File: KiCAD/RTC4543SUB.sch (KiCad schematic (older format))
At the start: 22 parts, among them J1 YM2203-B A-CON, J2 RTC-4543SA Mod, J3 I2C(Grove), J4 YM2203-B B-CON, Q1 2N7000, Q2 2N7000, U1 74HC07, U2 LP2950-3.3_TO92

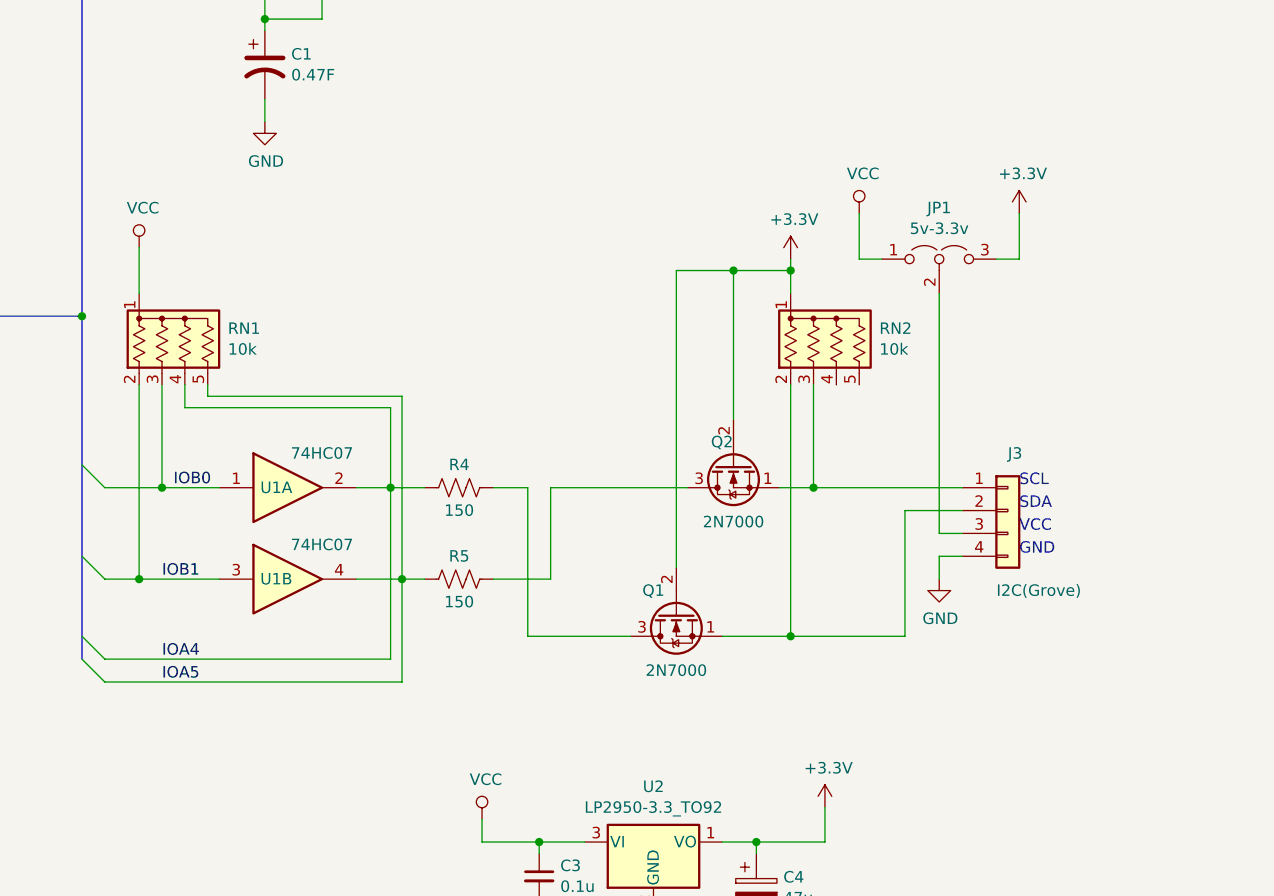
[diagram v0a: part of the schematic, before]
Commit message: I2C 電圧レベル変換を秋月電子AE-PCA9306モジュールへ変更
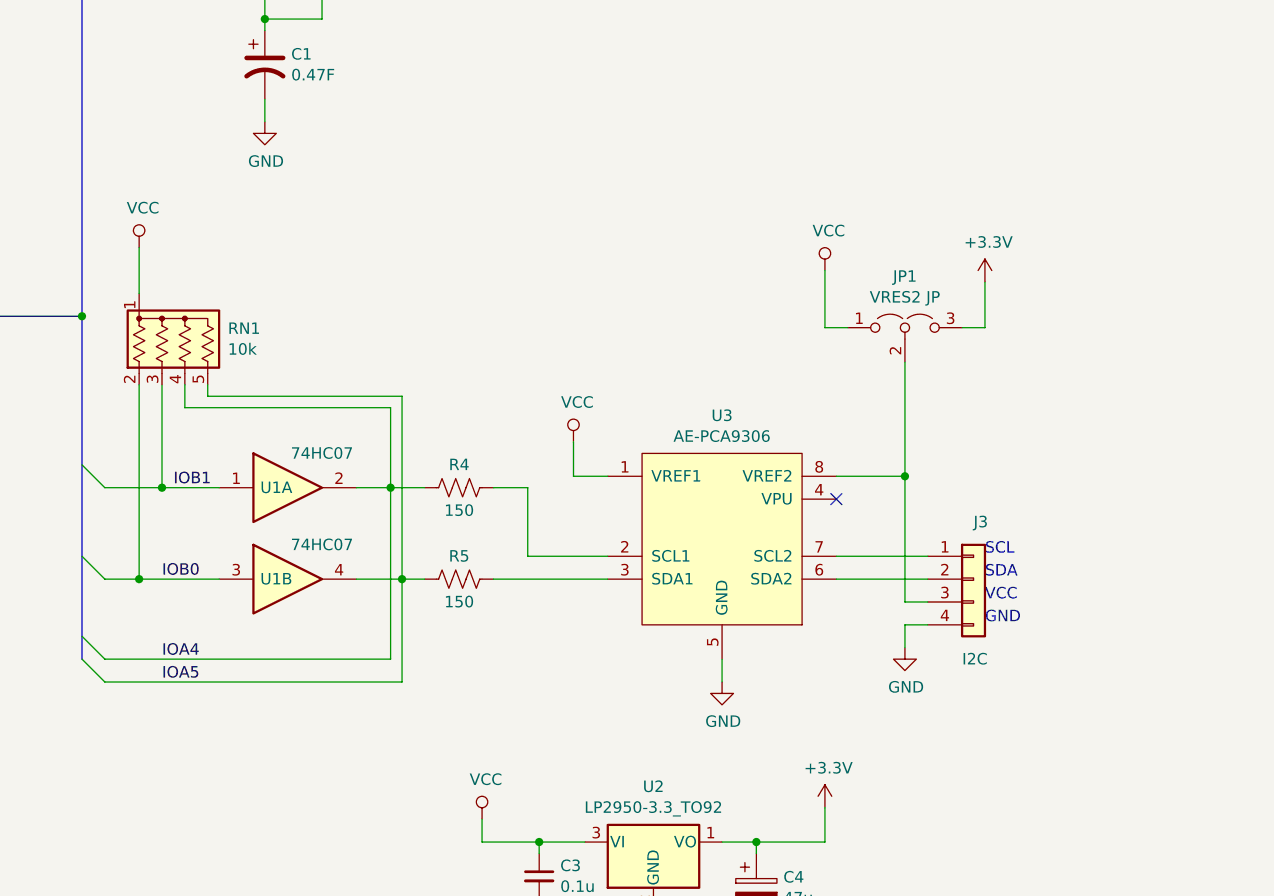
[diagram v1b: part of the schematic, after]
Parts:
- removed Q1, Q2: 2N7000, Package_TO_SOT_THT:TO-92_Inline, symbol Transistor_FET:2N7000
- removed RN2: 10k, Resistor_THT:R_Array_SIP5, symbol Device:R_Network04_US
- added U3: AE-PCA9306, symbol AE-PCA9306:AE-PCA9306
- J3: value I2C(Grove) -> I2C
- JP1: value 5v-3.3v -> VRES2 JP
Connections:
- net GND: now also U3.5 (GND)
- net IOB0: now also RN1.2 (R1), U1.3; no longer RN1.3 (R2), U1.1
- net IOB1: now also RN1.3 (R2), U1.1; no longer RN1.2 (R1), U1.3
- net VCC: now also U3.1 (VREF1)
- net at J3.1 (Pin_1): now also U3.7 (SCL2)
- net at J3.2 (Pin_2): now also U3.6 (SDA2)
- net at J3.3 (Pin_3), JP1.2 (C): now also U3.8 (VREF2)
- net at R4.1: now also U3.2 (SCL1)
- net at R5.1: now also U3.3 (SDA1)
- no-connect marks 24 -> 25
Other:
- moved on the sheet: J3
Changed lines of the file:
@@
 $EndComp
 Wire Wire Line
-	6350 5700 6350 5800
-Wire Wire Line
-	6450 5700 6350 5700
-Wire Wire Line
-	6350 5600 6450 5600
-$Comp
-L power:VCC #PWR09
-U 1 1 607028FD
-P 6000 4200
-F 0 "#PWR09" H 6000 4050 50  0001 C CNN
-F 1 "VCC" H 6017 4373 50  0000 C CNN
-F 2 "" H 6000 4200 50  0001 C CNN
-F 3 "" H 6000 4200 50  0001 C CNN
-	1    6000 4200
-	1    0    0    -1
-$EndComp
-Wire Wire Line
-	4650 5800 4650 5400
-Wire Wire Line
-	4400 5800 4650 5800
-Wire Wire Line
-	6200 5500 6450 5500
+	6200 6000 6200 6100
+Wire Wire Line
+	6300 6000 6200 6000
+Wire Wire Line
+	6200 5900 6300 5900
 Wire Wire Line
 	4400 5400 4550 5400
@@
 IOA5
 Text Label 2950 5800 0    50   ~ 0
-IOB1
+IOB0
 Wire Wire Line
 	2700 5800 2850 5800
@@
 IOA4
 Text Label 3000 5400 0    50   ~ 0
-IOB0
+IOB1
 Wire Wire Line
 	2700 5400 2950 5400
@@
 L power:GND #PWR010
 U 1 1 606C2B45
-P 6350 5800
-F 0 "#PWR010" H 6350 5550 50  0001 C CNN
-F 1 "GND" H 6355 5627 50  0000 C CNN
-F 2 "" H 6350 5800 50  0001 C CNN
-F 3 "" H 6350 5800 50  0001 C CNN
-	1    6350 5800
+P 6200 6100
+F 0 "#PWR010" H 6200 5850 50  0001 C CNN
+F 1 "GND" H 6205 5927 50  0000 C CNN
+F 2 "" H 6200 6100 50  0001 C CNN
+F 3 "" H 6200 6100 50  0001 C CNN
+	1    6200 6100
 	1    0    0    -1
 $EndComp
@@
 	1    0    0    -1
 $EndComp
-Text Notes 6700 5700 0    50   ~ 0
+Text Notes 6550 6000 0    50   ~ 0
 GND
-Text Notes 6700 5600 0    50   ~ 0
+Text Notes 6550 5900 0    50   ~ 0
 VCC
-Text Notes 6700 5500 0    50   ~ 0
+Text Notes 6550 5800 0    50   ~ 0
 SDA
-Text Notes 6700 5400 0    50   ~ 0
+Text Notes 6550 5700 0    50   ~ 0
 SCL
 $Comp
 L Connector_Generic:Conn_01x04 J3
 U 1 1 606BD3C7
-P 6650 5500
-F 0 "J3" H 6650 5750 50  0000 L CNN
-F 1 "I2C(Grove)" H 6600 5150 50  0000 L CNN
-F 2 "Connectors:Grove_1x04" H 6650 5500 50  0001 C CNN
-F 3 "~" H 6650 5500 50  0001 C CNN
-	1    6650 5500
+P 6500 5800
+F 0 "J3" H 6500 6050 50  0000 L CNN
+F 1 "I2C" H 6450 5450 50  0000 L CNN
+F 2 "Connectors:Grove_1x04" H 6500 5800 50  0001 C CNN
+F 3 "~" H 6500 5800 50  0001 C CNN
+	1    6500 5800
 	1    0    0    -1
 $EndComp
@@
 	1    0    0    -1
 $EndComp
-$Comp
-L Transistor_FET:2N7000 Q1
-U 1 1 6076870C
-P 5200 5950
-F 0 "Q1" V 5100 6050 50  0000 C CNN
-F 1 "2N7000" V 5450 5950 50  0000 C CNN
-F 2 "Package_TO_SOT_THT:TO-92_Inline" H 5400 5875 50  0001 L CIN
-F 3 "https://www.fairchildsemi.com/datasheets/2N/2N7000.pdf" H 5200 5950 50  0001 L CNN
-	1    5200 5950
-	0    -1   1    0
-$EndComp
-$Comp
-L power:+3.3V #PWR0103
-U 1 1 6076E120
-P 5700 4400
-F 0 "#PWR0103" H 5700 4250 50  0001 C CNN
-F 1 "+3.3V" H 5715 4573 50  0000 C CNN
-F 2 "" H 5700 4400 50  0001 C CNN
-F 3 "" H 5700 4400 50  0001 C CNN
-	1    5700 4400
-	1    0    0    -1
-$EndComp
-$Comp
-L Device:R_Network04_US RN2
-U 1 1 6076FE3F
-P 5900 4750
-F 0 "RN2" H 6088 4796 50  0000 L CNN
-F 1 "10k" H 6088 4705 50  0000 L CNN
-F 2 "Resistor_THT:R_Array_SIP5" V 6175 4750 50  0001 C CNN
-F 3 "http://www.vishay.com/docs/31509/csc.pdf" H 5900 4750 50  0001 C CNN
-	1    5900 4750
-	1    0    0    -1
-$EndComp
-$Comp
-L Transistor_FET:2N7000 Q2
-U 1 1 60777F0B
-P 5450 5300
-F 0 "Q2" V 5350 5350 50  0000 C CNN
-F 1 "2N7000" V 5700 5300 50  0000 C CNN
-F 2 "Package_TO_SOT_THT:TO-92_Inline" H 5650 5225 50  0001 L CIN
-F 3 "https://www.fairchildsemi.com/datasheets/2N/2N7000.pdf" H 5450 5300 50  0001 L CNN
-	1    5450 5300
-	0    -1   1    0
-$EndComp
-Wire Wire Line
-	4550 6050 5000 6050
-Wire Wire Line
-	4550 5400 4550 6050
-Wire Wire Line
-	4650 5400 5250 5400
+Wire Wire Line
+	4550 5400 4550 5700
 $Comp
 L power:+3.3V #PWR0104
 U 1 1 607AE270
-P 6700 4200
-F 0 "#PWR0104" H 6700 4050 50  0001 C CNN
-F 1 "+3.3V" H 6715 4373 50  0000 C CNN
-F 2 "" H 6700 4200 50  0001 C CNN
-F 3 "" H 6700 4200 50  0001 C CNN
-	1    6700 4200
-	1    0    0    -1
-$EndComp
-$Comp
-L Jumper:Jumper_3_Open JP1
-U 1 1 607AF803
-P 6350 4400
-F 0 "JP1" H 6350 4624 50  0000 C CNN
-F 1 "5v-3.3v" H 6350 4533 50  0000 C CNN
-F 2 "" H 6350 4400 50  0001 C CNN
-F 3 "~" H 6350 4400 50  0001 C CNN
-	1    6350 4400
-	1    0    0    -1
-$EndComp
-Wire Wire Line
-	6000 4200 6000 4400
-Wire Wire Line
-	6700 4400 6700 4200
+P 6550 4500
+F 0 "#PWR0104" H 6550 4350 50  0001 C CNN
+F 1 "+3.3V" H 6565 4673 50  0000 C CNN
+F 2 "" H 6550 4500 50  0001 C CNN
+F 3 "" H 6550 4500 50  0001 C CNN
+	1    6550 4500
+	1    0    0    -1
+$EndComp
+Wire Wire Line
+	6550 4700 6550 4500
 $Comp
 L power:+3.3V #PWR0105
@@
 $EndComp
 Wire Wire Line
-	6200 5500 6200 6050
-Wire Wire Line
-	5650 5400 5800 5400
-Wire Wire Line
-	5700 4400 5700 4450
-Wire Wire Line
-	5800 4950 5800 5400
-Connection ~ 5800 5400
-Wire Wire Line
-	5800 5400 6450 5400
-Connection ~ 5700 6050
-Wire Wire Line
-	5700 6050 6200 6050
-Wire Wire Line
-	5400 6050 5700 6050
-Wire Wire Line
-	5450 5100 5450 4450
-Wire Wire Line
-	5450 4450 5700 4450
-Connection ~ 5700 4450
-Wire Wire Line
-	5700 4450 5700 4550
-Wire Wire Line
-	5450 4450 5200 4450
-Wire Wire Line
-	5200 4450 5200 5750
-Connection ~ 5450 4450
-Wire Wire Line
-	5700 4950 5700 6050
-Wire Wire Line
-	6000 4400 6100 4400
-Wire Wire Line
-	6600 4400 6700 4400
-Wire Wire Line
-	6350 4550 6350 5600
+	6450 4700 6550 4700
 $Comp
 L Regulator_Linear:LP2950-3.3_TO92 U2
@@
 NoConn ~ 1700 5150
 Connection ~ 2600 4650
+$Comp
+L power:VCC #PWR09
+U 1 1 607ACB7D
+P 4750 5200
+F 0 "#PWR09" H 4750 5050 50  0001 C CNN
+F 1 "VCC" H 4767 5373 50  0000 C CNN
+F 2 "" H 4750 5200 50  0001 C CNN
+F 3 "" H 4750 5200 50  0001 C CNN
+	1    4750 5200
+	1    0    0    -1
+$EndComp
+$Comp
+L AE-PCA9306:AE-PCA9306 U3
+U 1 1 607B1CA9
+P 5400 5650
+F 0 "U3" H 5400 6215 50  0000 C CNN
+F 1 "AE-PCA9306" H 5400 6124 50  0000 C CNN
+F 2 "" H 5400 5500 50  0001 C CNN
+F 3 "" H 5400 5500 50  0001 C CNN
+	1    5400 5650
+	1    0    0    -1
+$EndComp
+Wire Wire Line
+	4400 5800 4900 5800
+Wire Wire Line
+	4550 5700 4900 5700
+Wire Wire Line
+	5900 5800 6300 5800
+Wire Wire Line
+	5900 5700 6300 5700
+NoConn ~ 5900 5450
+Wire Wire Line
+	4750 5200 4750 5350
+Wire Wire Line
+	4750 5350 4900 5350
+$Comp
+L power:VCC #PWR016
+U 1 1 607DA581
+P 5850 4450
+F 0 "#PWR016" H 5850 4300 50  0001 C CNN
+F 1 "VCC" H 5867 4623 50  0000 C CNN
+F 2 "" H 5850 4450 50  0001 C CNN
+F 3 "" H 5850 4450 50  0001 C CNN
+	1    5850 4450
+	1    0    0    -1
+$EndComp
+Wire Wire Line
+	5900 5350 6200 5350
+Wire Wire Line
+	6200 4850 6200 5350
+Connection ~ 6200 5350
+Wire Wire Line
+	6200 5350 6200 5900
+$Comp
+L Jumper:Jumper_3_Open JP1
+U 1 1 607E2E4E
+P 6200 4700
+F 0 "JP1" H 6200 4924 50  0000 C CNN
+F 1 "VRES2 JP" H 6200 4833 50  0000 C CNN
+F 2 "" H 6200 4700 50  0001 C CNN
+F 3 "~" H 6200 4700 50  0001 C CNN
+	1    6200 4700
+	1    0    0    -1
+$EndComp
+Wire Wire Line
+	5850 4450 5850 4700
+Wire Wire Line
+	5850 4700 5950 4700
+Wire Wire Line
+	5400 6150 5400 6250
+$Comp
+L power:GND #PWR015
+U 1 1 607F055E
+P 5400 6250
+F 0 "#PWR015" H 5400 6000 50  0001 C CNN
+F 1 "GND" H 5405 6077 50  0000 C CNN
+F 2 "" H 5400 6250 50  0001 C CNN
+F 3 "" H 5400 6250 50  0001 C CNN
+	1    5400 6250
+	1    0    0    -1
+$EndComp
 Wire Bus Line
 	3150 1250 3150 1850
